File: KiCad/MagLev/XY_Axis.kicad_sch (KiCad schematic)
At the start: 35 parts, among them Q1 ZX5T851GTA, Q2 ZX5T1951GTA, Q3 ZX5T851GTA, Q4 ZX5T1951GTA, U1 LM324

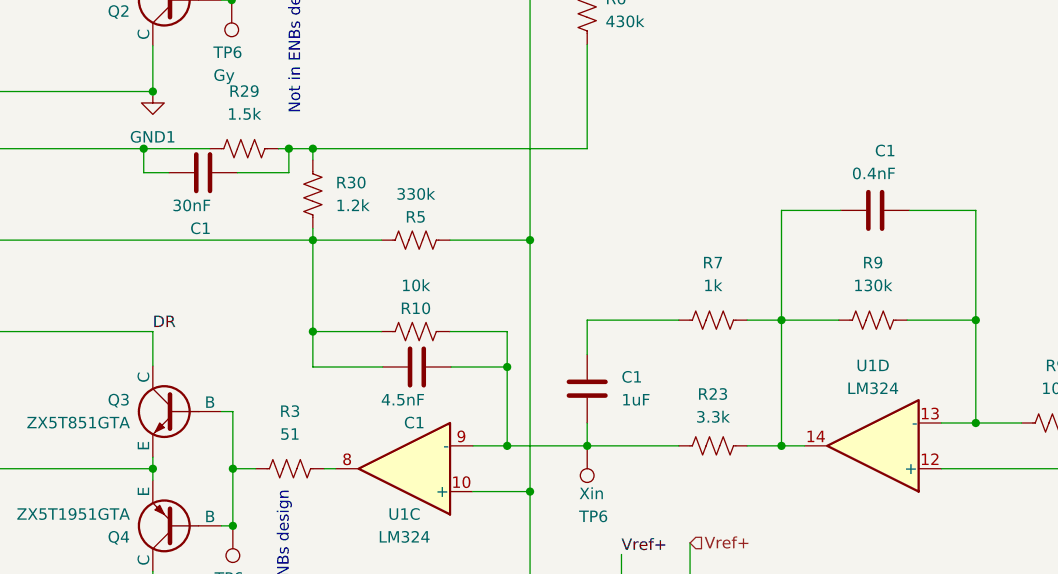
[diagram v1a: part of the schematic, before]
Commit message: Update BOM with JLCPCB PNs.
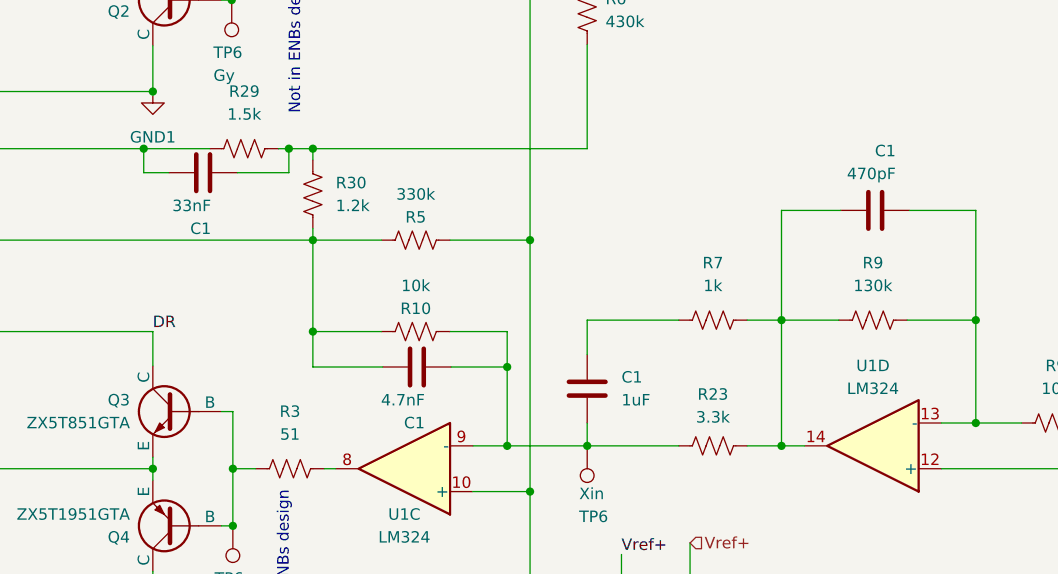
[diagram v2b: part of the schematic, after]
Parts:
- C1: JLC Part Number (none) -> C28323
- C1: value 30nF -> 33nF; JLC Part Number (none) -> C1739
- C1: value 0.4nF -> 470pF; JLC Part Number (none) -> C1743
- C1: value 4.5nF -> 4.7nF; JLC Part Number (none) -> C1744
- C2, C3: JLC Part Number (none) -> C249974
- D1, D2, D3, D4: JLC Part Number (none) -> C2480
- Q1, Q3: JLC Part Number (none) -> C99985
- R10, R9: JLC Part Number (none) -> C17414
- R2, R3: JLC Part Number (none) -> C17738
- R23: JLC Part Number (none) -> C465481
- R25, R7, R9: JLC Part Number (none) -> C17513
- R29: JLC Part Number (none) -> C2907216
- R30: JLC Part Number (none) -> C103956
- R5: JLC Part Number (none) -> C17629
- R6: JLC Part Number (none) -> C2930199
- R9: JLC Part Number (none) -> C2933305
- U1: JLC Part Number (none) -> C7943
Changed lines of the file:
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@@
       (effects (font (size 1.27 1.27)) hide)
     )
-    (property "JLC Part Number" "" (at 161.036 53.975 0)
+    (property "JLC Part Number" "C2930199" (at 161.036 53.975 0)
       (effects (font (size 1.27 1.27)) hide)
     )
@@
       (effects (font (size 1.27 1.27)) hide)
     )
-    (property "JLC Part Number" "" (at 161.036 96.012 0)
+    (property "JLC Part Number" "C28323" (at 161.036 96.012 0)
       (effects (font (size 1.27 1.27)) hide)
     )
@@
       (effects (font (size 1.27 1.27)) hide)
     )
-    (property "JLC Part Number" "" (at 184.658 141.986 0)
+    (property "JLC Part Number" "C17513" (at 184.658 141.986 0)
       (effects (font (size 1.27 1.27)) hide)
     )
@@
       (effects (font (size 1.27 1.27)) hide)
     )
-    (property "JLC Part Number" "" (at 41.148 65.532 0)
+    (property "JLC Part Number" "C7943" (at 41.148 65.532 0)
       (effects (font (size 1.27 1.27)) hide)
     )
@@
       (effects (font (size 1.27 1.27)) hide)
     )
-    (property "JLC Part Number" "" (at 192.786 102.362 0)
+    (property "JLC Part Number" "C7943" (at 192.786 102.362 0)
       (effects (font (size 1.27 1.27)) hide)
     )
@@
       (effects (font (size 1.27 1.27)) hide)
     )
-    (property "JLC Part Number" "" (at 122.936 69.342 0)
+    (property "JLC Part Number" "C2907216" (at 122.936 69.342 0)
       (effects (font (size 1.27 1.27)) hide)
     )
@@
       (effects (font (size 1.27 1.27)) hide)
     )
-    (property "JLC Part Number" "" (at 184.658 129.54 0)
+    (property "JLC Part Number" "C17513" (at 184.658 129.54 0)
       (effects (font (size 1.27 1.27)) hide)
     )
@@
       (effects (font (size 1.27 1.27)) hide)
     )
-    (property "JLC Part Number" "" (at 128.016 46.482 0)
+    (property "JLC Part Number" "C17738" (at 128.016 46.482 0)
       (effects (font (size 1.27 1.27)) hide)
     )
@@
       (effects (font (size 1.27 1.27)) hide)
     )
-    (property "JLC Part Number" "" (at 37.465 95.504 0)
+    (property "JLC Part Number" "C7943" (at 37.465 95.504 0)
       (effects (font (size 1.27 1.27)) hide)
     )
@@
       (effects (font (size 1.27 1.27)) hide)
     )
-    (property "JLC Part Number" "" (at 221.996 116.332 0)
+    (property "JLC Part Number" "C17513" (at 221.996 116.332 0)
       (effects (font (size 1.27 1.27)) hide)
     )
@@
       (effects (font (size 1.27 1.27)) (justify left))
     )
-    (property "Value" "30nF" (at 119.253 75.692 90)
+    (property "Value" "33nF" (at 119.253 75.692 90)
       (effects (font (size 1.27 1.27)) (justify left))
     )
@@
       (effects (font (size 1.27 1.27)) hide)
     )
-    (property "JLC Part Number" "" (at 118.364 72.009 0)
+    (property "JLC Part Number" "C1739" (at 118.364 72.009 0)
       (effects (font (size 1.27 1.27)) hide)
     )
@@
       (effects (font (size 1.27 1.27)) hide)
     )
-    (property "JLC Part Number" "" (at 93.726 112.522 0)
+    (property "JLC Part Number" "C2480" (at 93.726 112.522 0)
       (effects (font (size 1.27 1.27)) hide)
     )
@@
       (effects (font (size 1.27 1.27)) hide)
     )
-    (property "JLC Part Number" "" (at 172.466 142.367 0)
+    (property "JLC Part Number" "C249974" (at 172.466 142.367 0)
       (effects (font (size 1.27 1.27)) hide)
     )
@@
       (effects (font (size 1.27 1.27)) hide)
     )
-    (property "JLC Part Number" "" (at 175.006 88.392 0)
+    (property "JLC Part Number" "C17513" (at 175.006 88.392 0)
       (effects (font (size 1.27 1.27)) hide)
     )
@@
       (effects (font (size 1.27 1.27)) (justify left))
     )
-    (property "Value" "0.4nF" (at 195.326 72.136 90)
+    (property "Value" "470pF" (at 195.326 72.136 90)
       (effects (font (size 1.27 1.27)) (justify left))
     )
@@
       (effects (font (size 1.27 1.27)) hide)
     )
-    (property "JLC Part Number" "" (at 193.04 76.2 0)
+    (property "JLC Part Number" "C1743" (at 193.04 76.2 0)
       (effects (font (size 1.27 1.27)) hide)
     )
@@
       (effects (font (size 1.27 1.27)) hide)
     )
-    (property "JLC Part Number" "" (at 175.006 102.362 0)
+    (property "JLC Part Number" "C465481" (at 175.006 102.362 0)
       (effects (font (size 1.27 1.27)) hide)
     )
@@
       (effects (font (size 1.27 1.27)) hide)
     )
-    (property "JLC Part Number" "" (at 192.786 88.392 0)
+    (property "JLC Part Number" "C2933305" (at 192.786 88.392 0)
       (effects (font (size 1.27 1.27)) hide)
     )
@@
       (effects (font (size 1.27 1.27)) hide)
     )
-    (property "JLC Part Number" "" (at 93.726 38.862 0)
+    (property "JLC Part Number" "C2480" (at 93.726 38.862 0)
       (effects (font (size 1.27 1.27)) hide)
     )
@@
       (effects (font (size 1.27 1.27)) hide)
     )
-    (property "JLC Part Number" "" (at 221.996 126.492 0)
+    (property "JLC Part Number" "C17513" (at 221.996 126.492 0)
       (effects (font (size 1.27 1.27)) hide)
     )
@@
       (effects (font (size 1.27 1.27)) hide)
     )
-    (property "JLC Part Number" "" (at 93.726 54.102 0)
+    (property "JLC Part Number" "C2480" (at 93.726 54.102 0)
       (effects (font (size 1.27 1.27)) hide)
     )
@@
       (effects (font (size 1.27 1.27)) hide)
     )
-    (property "JLC Part Number" "" (at 213.106 99.822 0)
+    (property "JLC Part Number" "C17414" (at 213.106 99.822 0)
       (effects (font (size 1.27 1.27)) hide)
     )
@@
       (effects (font (size 1.27 1.27)) hide)
     )
-    (property "JLC Part Number" "" (at 140.716 104.902 0)
+    (property "JLC Part Number" "C7943" (at 140.716 104.902 0)
       (effects (font (size 1.27 1.27)) hide)
     )
@@
       (effects (font (size 1.27 1.27)) hide)
     )
-    (property "JLC Part Number" "" (at 172.466 129.667 0)
+    (property "JLC Part Number" "C249974" (at 172.466 129.667 0)
       (effects (font (size 1.27 1.27)) hide)
     )
@@
       (effects (font (size 1.27 1.27)) (justify left))
     )
-    (property "Value" "4.5nF" (at 143.002 97.282 90)
+    (property "Value" "4.7nF" (at 143.002 97.282 90)
       (effects (font (size 1.27 1.27)) (justify left))
     )
@@
       (effects (font (size 1.27 1.27)) hide)
     )
-    (property "JLC Part Number" "" (at 142.113 93.599 0)
+    (property "JLC Part Number" "C1744" (at 142.113 93.599 0)
       (effects (font (size 1.27 1.27)) hide)
     )
@@
       (effects (font (size 1.27 1.27)) hide)
     )
-    (property "JLC Part Number" "" (at 115.316 98.552 0)
+    (property "JLC Part Number" "C99985" (at 115.316 98.552 0)
       (effects (font (size 1.27 1.27)) hide)
     )
@@
       (effects (font (size 1.27 1.27)) hide)
     )
-    (property "JLC Part Number" "" (at 141.986 79.502 0)
+    (property "JLC Part Number" "C17629" (at 141.986 79.502 0)
       (effects (font (size 1.27 1.27)) hide)
     )
@@
       (effects (font (size 1.27 1.27)) hide)
     )
-    (property "JLC Part Number" "" (at 93.726 97.282 0)
+    (property "JLC Part Number" "C2480" (at 93.726 97.282 0)
       (effects (font (size 1.27 1.27)) hide)
     )
@@
       (effects (font (size 1.27 1.27)) hide)
     )
-    (property "JLC Part Number" "" (at 141.986 89.662 0)
+    (property "JLC Part Number" "C17414" (at 141.986 89.662 0)
       (effects (font (size 1.27 1.27)) hide)
     )
@@
       (effects (font (size 1.27 1.27)) hide)
     )
-    (property "JLC Part Number" "" (at 130.556 74.422 0)
+    (property "JLC Part Number" "C103956" (at 130.556 74.422 0)
       (effects (font (size 1.27 1.27)) hide)
     )
@@
       (effects (font (size 1.27 1.27)) hide)
     )
-    (property "JLC Part Number" "" (at 128.016 104.902 0)
+    (property "JLC Part Number" "C17738" (at 128.016 104.902 0)
       (effects (font (size 1.27 1.27)) hide)
     )
@@
       (effects (font (size 1.27 1.27)) hide)
     )
-    (property "JLC Part Number" "" (at 140.716 46.482 0)
+    (property "JLC Part Number" "C7943" (at 140.716 46.482 0)
       (effects (font (size 1.27 1.27)) hide)
     )
@@
       (effects (font (size 1.27 1.27)) hide)
     )
-    (property "JLC Part Number" "" (at 115.316 40.132 0)
-      (effects (font (size 1.27 1.27)) hide)
-    )
+    (property "JLC Part Number" "C99985" (at 115.316 40.132 0)
+      (effects (font (size 1.27 1.27)) hide)
+    )

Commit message: Add board art folder and upload svg files.
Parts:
- R23: JLC Part Number C465481 -> C26010
- R29: JLC Part Number C2907216 -> C4310
- R30: JLC Part Number C103956 -> C17379
- RV2: value 10k -> 1k
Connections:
- net at U1.1: now also U1.2 (-)
- no-connect marks 3 -> 1
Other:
- moved on the sheet: U1A
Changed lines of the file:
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@@
   (junction (at 130.556 79.502) (diameter 0) (color 0 0 0 0)
   )
-  (no_connect (at 26.035 95.504))
-  (no_connect (at 49.53 98.044))
-  (no_connect (at 49.53 92.964))
+  (no_connect (at 48.133 107.188))
   (wire (pts (xy 148.336 43.942) (xy 161.036 43.942))
     (stroke (width 0) (type default))
@@
     (stroke (width 0) (type default))
   )
-  (wire (pts (xy 45.085 98.044) (xy 49.53 98.044))
+  (wire (pts (xy 43.688 107.188) (xy 48.133 107.188))
     (stroke (width 0) (type default))
   )
@@
     (stroke (width 0) (type default))
   )
+  (wire (pts (xy 24.638 104.648) (xy 24.638 90.678))
+    (stroke (width 0) (type default))
+  )
   (wire (pts (xy 93.726 42.672) (xy 93.726 46.482))
     (stroke (width 0) (type default))
@@
     (stroke (width 0) (type default))
   )
+  (wire (pts (xy 24.638 90.678) (xy 48.514 90.678))
+    (stroke (width 0) (type default))
+  )
   (wire (pts (xy 81.026 46.482) (xy 93.726 46.482))
     (stroke (width 0) (type default))
@@
     (stroke (width 0) (type default))
   )
+  (wire (pts (xy 48.514 90.678) (xy 48.514 102.108))
+    (stroke (width 0) (type default))
+  )
   (wire (pts (xy 121.666 104.902) (xy 121.666 111.252))
     (stroke (width 0) (type default))
@@
     (stroke (width 0) (type default))
   )
-  (wire (pts (xy 45.085 92.964) (xy 49.53 92.964))
-    (stroke (width 0) (type default))
-  )
-  (wire (pts (xy 26.035 95.504) (xy 29.845 95.504))
+  (wire (pts (xy 43.688 102.108) (xy 48.514 102.108))
+    (stroke (width 0) (type default))
+  )
+  (wire (pts (xy 24.638 104.648) (xy 28.448 104.648))
     (stroke (width 0) (type default))
   )
@@
       (effects (font (size 1.27 1.27)) hide)
     )
-    (property "JLC Part Number" "C2907216" (at 122.936 69.342 0)
+    (property "JLC Part Number" "C4310" (at 122.936 69.342 0)
       (effects (font (size 1.27 1.27)) hide)
     )
@@
     )
   )
-  (symbol (lib_id "Amplifier_Operational:LM324") (at 37.465 95.504 180) (unit 1)
+  (symbol (lib_id "Amplifier_Operational:LM324") (at 36.068 104.648 180) (unit 1)
     (in_bom yes) (on_board yes) (dnp no) (fields_autoplaced)
-    (property "Reference" "U1" (at 37.465 85.344 0)
-      (effects (font (size 1.27 1.27)))
-    )
-    (property "Value" "LM324" (at 37.465 87.884 0)
-      (effects (font (size 1.27 1.27)))
-    )
-    (property "Footprint" "Package_SO:SOIC-14_3.9x8.7mm_P1.27mm" (at 38.735 98.044 0)
-      (effects (font (size 1.27 1.27)) hide)
-    )
-    (property "Datasheet" "http://www.ti.com/lit/ds/symlink/lm2902-n.pdf" (at 36.195 100.584 0)
-      (effects (font (size 1.27 1.27)) hide)
-    )
-    (property "JLC Part Number" "C7943" (at 37.465 95.504 0)
+    (property "Reference" "U1" (at 36.068 94.488 0)
+      (effects (font (size 1.27 1.27)))
+    )
+    (property "Value" "LM324" (at 36.068 97.028 0)
+      (effects (font (size 1.27 1.27)))
+    )
+    (property "Footprint" "Package_SO:SOIC-14_3.9x8.7mm_P1.27mm" (at 37.338 107.188 0)
+      (effects (font (size 1.27 1.27)) hide)
+    )
+    (property "Datasheet" "http://www.ti.com/lit/ds/symlink/lm2902-n.pdf" (at 34.798 109.728 0)
+      (effects (font (size 1.27 1.27)) hide)
+    )
+    (property "JLC Part Number" "C7943" (at 36.068 104.648 0)
       (effects (font (size 1.27 1.27)) hide)
     )
@@
       (effects (font (size 1.27 1.27)) (justify right))
     )
-    (property "Value" "10k" (at 230.886 120.142 0)
+    (property "Value" "1k" (at 230.886 120.142 0)
       (effects (font (size 1.27 1.27)) (justify right))
     )
@@
       (effects (font (size 1.27 1.27)) hide)
     )
-    (property "JLC Part Number" "C465481" (at 175.006 102.362 0)
+    (property "JLC Part Number" "C26010" (at 175.006 102.362 0)
       (effects (font (size 1.27 1.27)) hide)
     )
@@
       (effects (font (size 1.27 1.27)) hide)
     )
-    (property "JLC Part Number" "C103956" (at 130.556 74.422 0)
-      (effects (font (size 1.27 1.27)) hide)
-    )
+    (property "JLC Part Number" "C17379" (at 130.556 74.422 0)
+      (effects (font (size 1.27 1.27)) hide)
+    )
